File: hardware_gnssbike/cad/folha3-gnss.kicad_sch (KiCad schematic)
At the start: 13 parts, among them J302 Hirose U.FL-R-SMT-1, U301 u-blox MAX-F10S

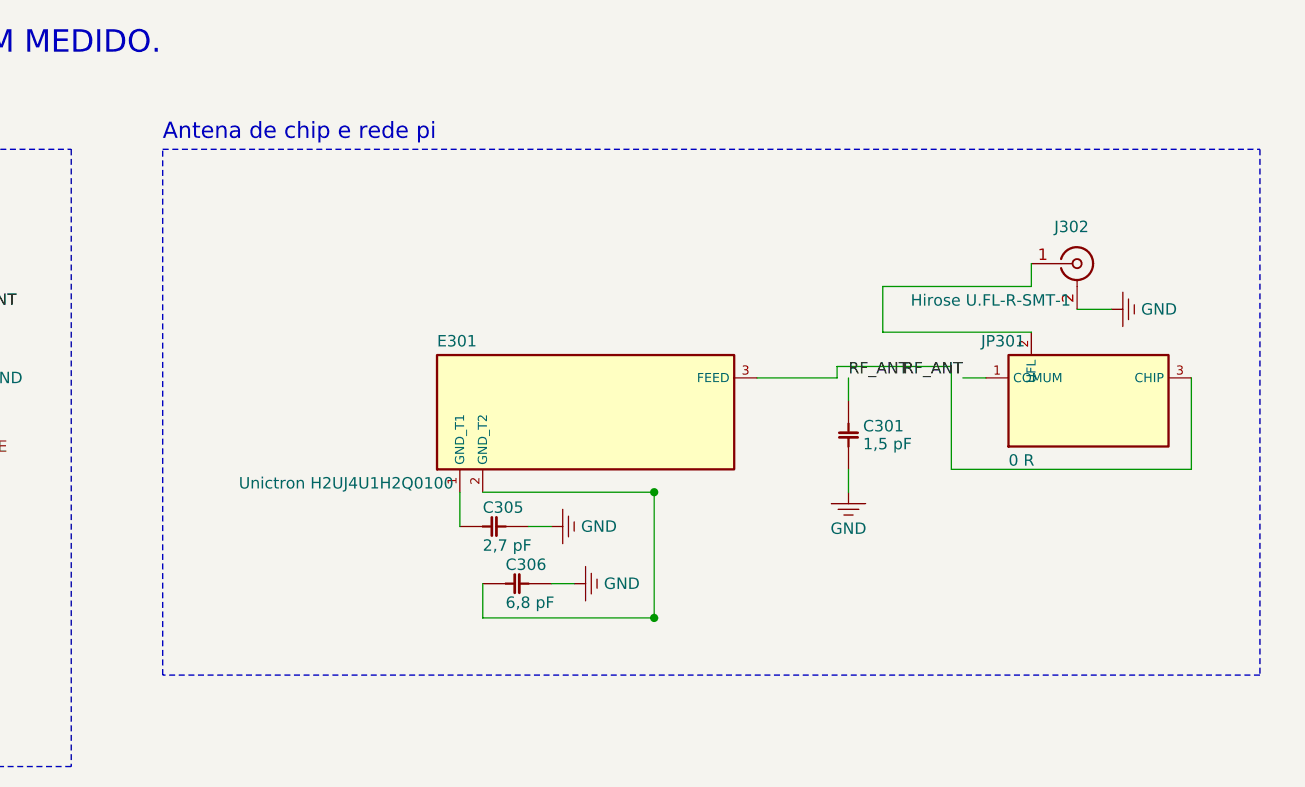
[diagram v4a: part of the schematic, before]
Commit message: feat(hardware): apply the schematic review, take either display, review the case
Apply the corrections the owner approved on 2026-10-18, in the
generators: the BMP585 land from figure 29, the RGB LED land unmirrored,
the TLV7031DCKR renumbered and fed from VBAT_SYS, the common pad of
JP301 in the middle, the OPT3001 exposed pad, the Murata land for the
buck inductors, 10 uF on PVDD and 3V3BL, a 24 V TVS on VBUS, the flash
on 3V0, pin-1 marks, the charge LEDs in the key row, the TVS next to
their connectors, the USB-C on the maker's edge line, the Same Sky
buzzer in place of the last-time-buy Murata, and an LCSC code on every
fitted part.

The board takes the JDI or the Sharp on one dual-contact Molex 503480:
JP401 picks 3V0 or 5V0, and a TPS610997 boost feeds the Sharp. A second
blind check found the connector drawn backwards (the tail enters on the
nail side); the land, the circuit order and the boost placement follow
the drawings now.

The router finds its way further: unique UUIDs per footprint, so the
DRC names the right pads; the chip antenna's own nets inside its
keep-out; JP301 turned so the two RF lines do not cross; ground vias
outside the dense chips, bent and geometrically checked ground stubs,
and a pass with the power rails first. The DRC reports no error; 60
items are still unconnected.

The case is reviewed part by part (hardware_gnssbike/12): the solar
module pockets follow the datasheet's +-0.3 mm (the case grows to 64 mm),
the keys stop 0.15 mm under the membrane, and the light sensor gets a
sealed window. The sealing of the USB-C, the floor holes and the lid
seam is left to the owner. The documents follow parts.py.

Nothing is fabricated, and the routing is still open.
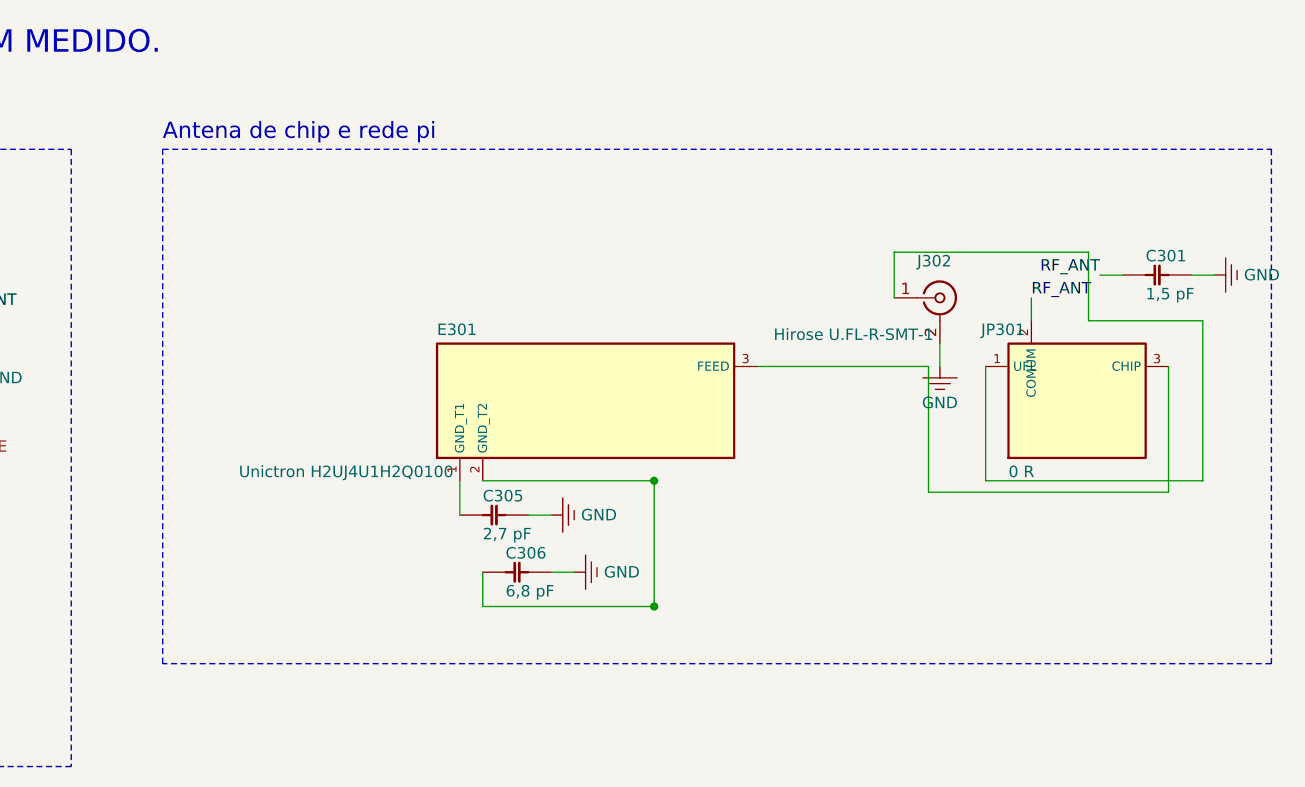
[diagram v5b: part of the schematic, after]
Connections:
- net RF_ANT: now also JP301.2 (COMUM); no longer JP301.1 (COMUM)
- net at J302.1 (In): now also JP301.1 (UFL); no longer JP301.2 (UFL)
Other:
- moved on the sheet: C301, C305, C306, E301, J302, JP301

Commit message: fix(hardware): change the schematic where the board could not route
Three changes the routing of 2026-10-19 asked for, each checked against
the part's datasheet:

- ALRT of the MAX17262 goes to GND, as the datasheet asks when the alert
  is not used, and its 10 k pull-up R110 is gone: no pin read it, and the
  middle bump of a 0.4 mm WLP could only reach it through a via in pad.
- The USB pair crosses the TPD4E05U06 by the channels in the order it
  arrives (D+ on pins 5 and 6, D- on 4 and 7). The four channels are the
  same diode to ground; with the pin names followed, the pair could only
  reach the module by crossing itself on a layer where it takes no via.
- The chip antenna's tuning capacitors sit where Unictron's figures 5-1
  and 8-1 put them, lying on the board edge at the two ends of the
  cut-out, with C305 (pin 1, wide side) at 6.8 pF and C306 at 2.7 pF.
  They stood in the middle of the cut-out with the values swapped, and
  the ground pad of C305 had no ground within reach.

check_sch.py regenerates the sheets and passes, with the open-drain ALRT
on the ground node accepted by the ERC; the schematic PDF is exported
again. Bench tuning of the antenna is still to be done.
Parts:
- C305: value 2,7 pF -> 6,8 pF
- C306: value 6,8 pF -> 2,7 pF
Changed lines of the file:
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@@
 			(effects (font (size 1.27 1.27)) (justify left bottom))
 		)
-		(property "Value" "2,7 pF"
+		(property "Value" "6,8 pF"
 			(at 148.590 76.296 0)
 			(effects (font (size 1.27 1.27)) (justify left top))
@@
 			(effects (font (size 1.27 1.27)) (hide yes))
 		)
-		(property "Description" "sintonia do pino 1 da antena ao terra; valor de partida da ficha, a ajustar na bancada"
+		(property "Description" "sintonia [9] do pino 1 da antena ao terra, na ponta do lado largo do recorte; valor de partida da ficha, a ajustar na bancada"
 			(at 149.86 74.93 0)
 			(effects (font (size 1.27 1.27)) (hide yes))
@@
 			(effects (font (size 1.27 1.27)) (justify left bottom))
 		)
-		(property "Value" "6,8 pF"
+		(property "Value" "2,7 pF"
 			(at 151.130 82.646 0)
 			(effects (font (size 1.27 1.27)) (justify left top))
@@
 			(effects (font (size 1.27 1.27)) (hide yes))
 		)
-		(property "Description" "sintonia do pino 2 da antena ao terra; valor de partida da ficha, a ajustar na bancada"
+		(property "Description" "sintonia [8] do pino 2 da antena ao terra, na ponta do lado estreito do recorte; valor de partida da ficha, a ajustar na bancada"
 			(at 152.4 81.28 0)
 			(effects (font (size 1.27 1.27)) (hide yes))

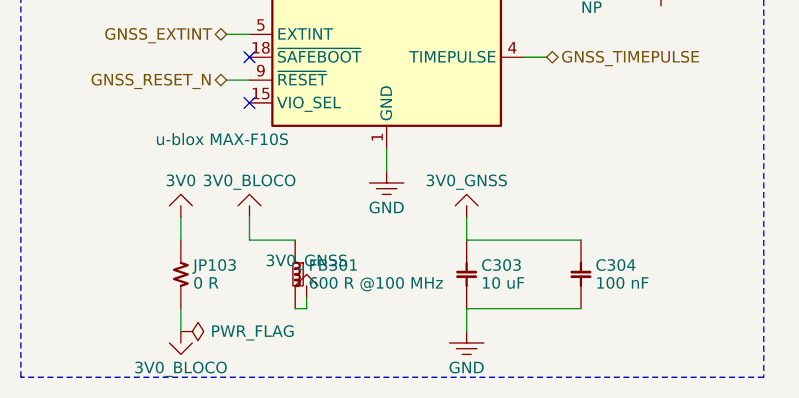
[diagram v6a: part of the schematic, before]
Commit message: fix(hardware): lower-DCR ferrite on the GNSS supply
The MAX-F10S integration manual (4.1.1) allows 0.2 ohm in series on
VCC. Measured on the routed board, the copper from the BUCK2 inductor to
the pin is 69 mOhm, mostly on the 0.5 oz inner layer, and the JP103
current jumper adds up to 50: with the BLM18KG601SN1D (150 mOhm max) the
worst case was 275 mOhm. The BLM18KG221SN1D of the same Murata series
(LCSC C88980; 220 ohm at 100 MHz, 2.2 A, 50 mOhm max) brings it to 169.

check_sch.py regenerates the GNSS sheet and passes; the schematic PDF is
exported again, and the shopping list and BOM carry the new part.
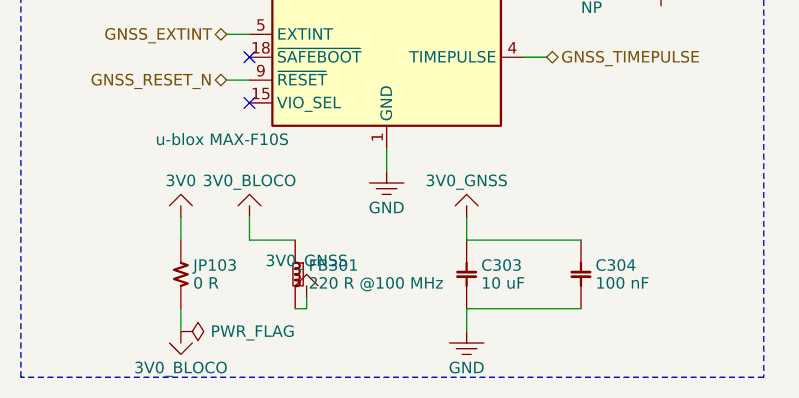
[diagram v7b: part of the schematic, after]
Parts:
- FB301: value 600 R @100 MHz -> 220 R @100 MHz
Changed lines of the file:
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@@
 			(effects (font (size 1.27 1.27)) (justify left bottom))
 		)
-		(property "Value" "600 R @100 MHz"
+		(property "Value" "220 R @100 MHz"
 			(at 52.289 91.690 90)
 			(effects (font (size 1.27 1.27)) (justify left top))
@@
 			(effects (font (size 1.27 1.27)) (hide yes))
 		)
-		(property "Description" "ferrite do 3V0 junto do receptor: Murata BLM18KG601SN1D, 0603, 1,3 A, DCR 150 mOhm - dentro dos 0,2 ohm do manual (4.1.1). Fechado em 2026-09-25; era o BLM15PX601SN1D de 0402 e 230 mOhm"
+		(property "Description" "ferrite do 3V0 junto do receptor: Murata BLM18KG221SN1D, 0603, 2,2 A, DCR maximo 50 mOhm - com o cobre e o JP103, 175 mOhm dos 0,2 ohm do manual (4.1.1). Trocada em 2026-10-19; era a BLM18KG601SN1D, 150 mOhm"
 			(at 50.8 91.44 0)
 			(effects (font (size 1.27 1.27)) (hide yes))
